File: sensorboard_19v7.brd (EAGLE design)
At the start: 100 x 58 mm, 105 parts, among them IC1 ECMF02-2AMX6, IC2_ESP32S2WROOMM22S2 ESP32-S2-WROOM_M22S2H3200PH3Q0, IC4 TPA6211A1DRBR, J4_USB USB_CONN, J5_AUDIO SJ-3523-SMT-TR, J6_OAT 2.5mm JACK, J7 30310-6002HB, U1 LPS22HB, U10-MAG_SENSOR MMC5983MA, U11 LDL212PV33R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

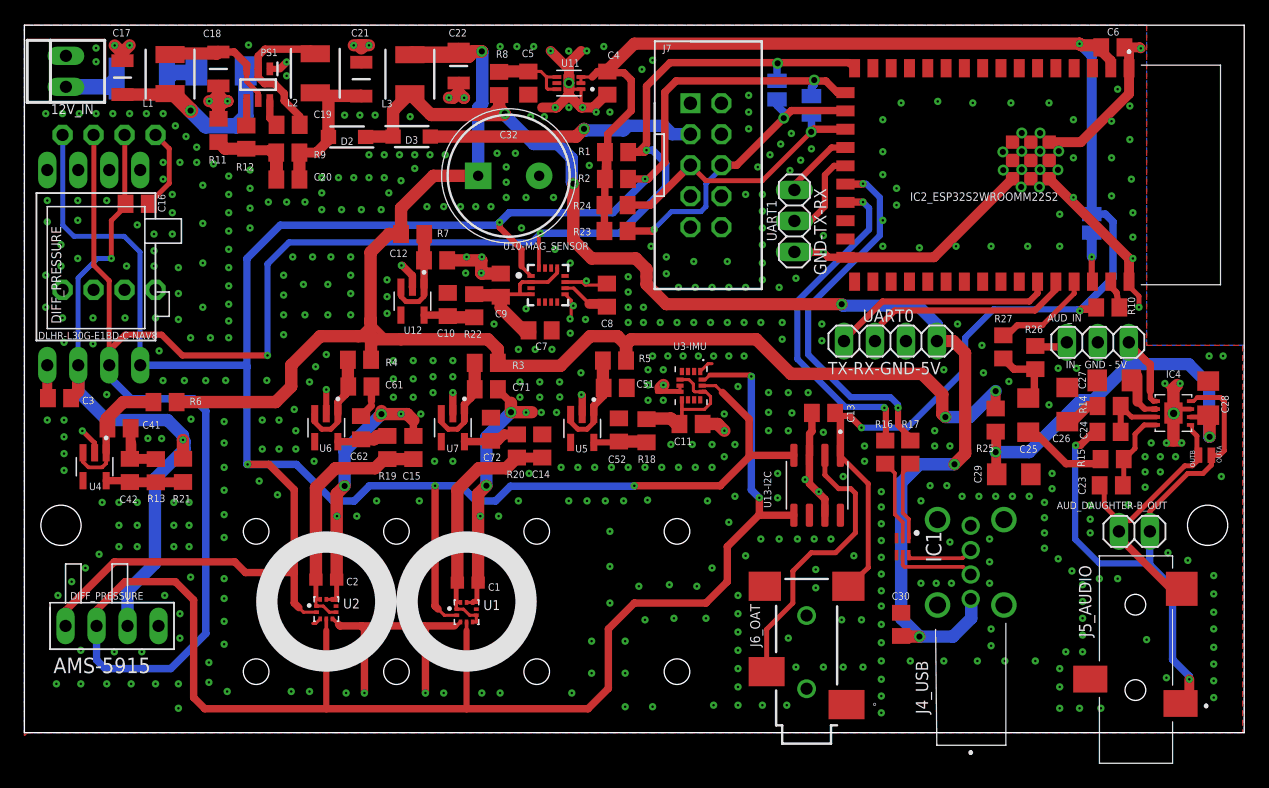
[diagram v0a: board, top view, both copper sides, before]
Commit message: Upload sensorboard_19 files
Increase via drill size
Change USB common mode filter to larger part
Add 6 pin header for SPI, 5V, GND
Add ESP32 EN pin bypass capacitor

Remove sensorboard_18 files
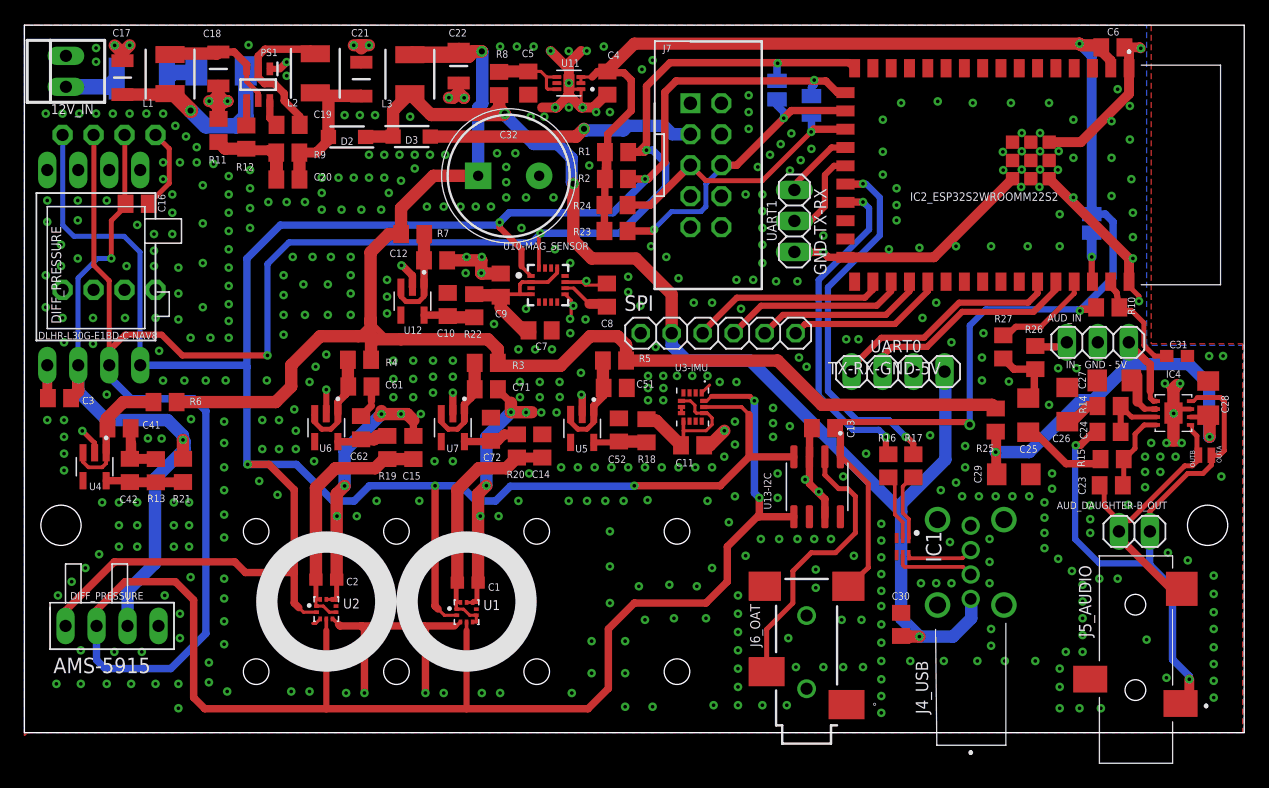
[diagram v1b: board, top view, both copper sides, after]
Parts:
- added C31: 100nF, rcl:C0603
- added SPI: (no value), pinhead_dD:1X06
- moved UART0 2.58 mm to (71.6, 29.6)
- moved C11 1.75 mm to (54.8, 23.6)
- moved U3-IMU 1.75 mm to (54.8, 26.7)
- moved C13 1.25 mm to (65.5, 25.0)
- moved R16 1.15 mm to (70.8, 21.9)
- moved R17 1.15 mm to (72.9, 21.9)
- moved U13-I2C 0.12 mm to (65.0, 20.2)
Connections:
- new net FSPICLK: IC2_ESP32S2WROOMM22S2.30, SPI.5
- new net FSPICS0: IC2_ESP32S2WROOMM22S2.28, SPI.3
- new net FSPID_MOSI: IC2_ESP32S2WROOMM22S2.29, SPI.4
- new net FSPIQ_MISO: IC2_ESP32S2WROOMM22S2.31, SPI.6
- net 5VD: now also SPI.2
- net GND: now also C31.2, SPI.1
- net N$7: now also C31.1
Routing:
- net FSPICS0: track 0.00 -> 16.2 mm
- net FSPID_MOSI: track 0.00 -> 15.1 mm
- net FSPICLK: track 0.00 -> 14.1 mm
- net FSPIQ_MISO: track 0.00 -> 13.0 mm
- net N$7: track 2.33 -> 8.95 mm
- net 5VC: track 131.0 -> 125.2 mm, vias 3 -> 1
- net GND: track 211.3 -> 207.2 mm, vias 578 -> 554
- net 5VD: track 112.9 -> 110.2 mm, vias 5 -> 3
- net SDA0: track 263.6 -> 261.9 mm
- net 3V3_DIG: track 134.3 -> 135.9 mm
- net N$28: track 6.69 -> 5.46 mm
- net N$27: track 6.57 -> 5.63 mm
- net USB_D+: track 28.6 -> 27.7 mm
- net VDD3F: track 11.6 -> 12.3 mm
- net SCL0: track 223.7 -> 223.0 mm
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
